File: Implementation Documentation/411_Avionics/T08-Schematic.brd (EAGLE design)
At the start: 65.8 x 25.4 mm, 68 parts, among them IC1 BQ24022, J1 USB-MICROB, J3 JST-PH-2-SMT-RA, U1 LP5907, U2 M25P10-AVMN6TP_TR, U3 LSM9DS0, U5 LTC1998, U6 ATMEGA32U4-AU, X1 8MHz

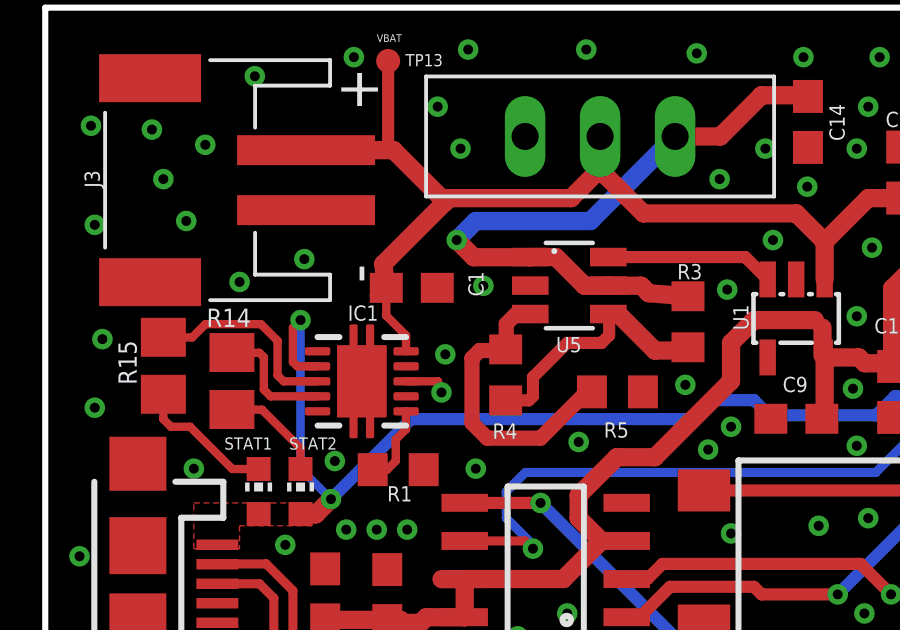
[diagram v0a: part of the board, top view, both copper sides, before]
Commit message: Rerouted /PG pin on BQ24022. Corrected symbol and added to eagle library.
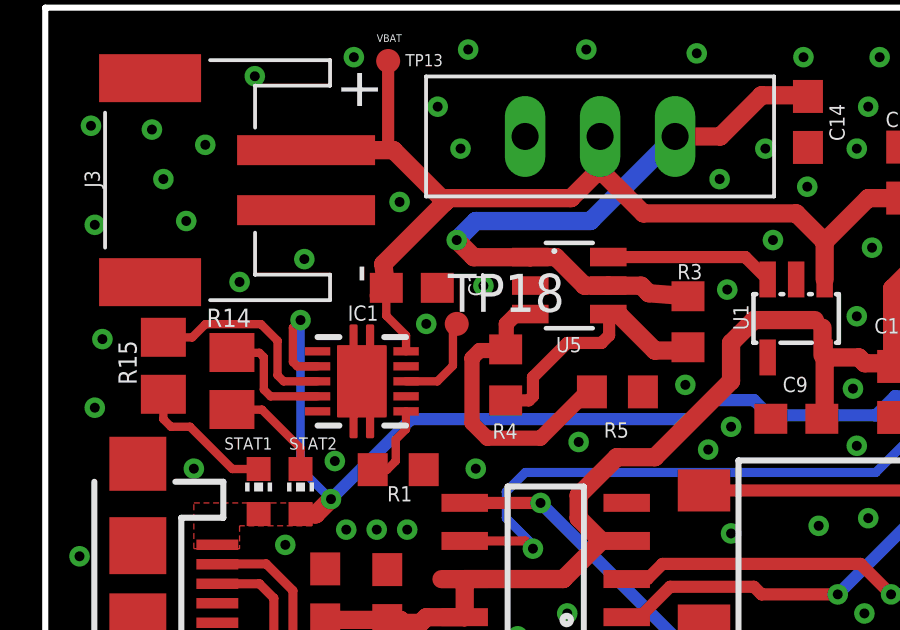
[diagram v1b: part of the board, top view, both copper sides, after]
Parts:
- added TP18: TPTP08R, testpad:TP08R
- IC1: device texas:DRC-S-PVSON-N10 -> tinyav-lib:DRC-S-PVSON-N10
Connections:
- new net N$68: IC1.8, TP18.TP
- net GND: no longer IC1.8
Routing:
- net N$68: track 0.00 -> 3.23 mm
- net GND: track 5.75 -> 4.30 mm
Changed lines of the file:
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@@
 <attribute name="NAME" x="41.906" y="24.562" size="0.508" layer="25" rot="R180"/>
 </element>
-<element name="IC1" library="texas" package="DRC-S-PVSON-N10" value="BQ24022" x="10.552" y="12.944" smashed="yes" rot="R270">
+<element name="IC1" library="tinyav-lib" package="DRC-S-PVSON-N10" value="BQ24022" x="10.552" y="12.944" smashed="yes" rot="R270">
 <attribute name="NAME" x="10.083" y="14.965" size="0.508" layer="25"/>
 </element>
@@
 <attribute name="VALUE" x="53.721" y="21.336" size="0.0254" layer="27"/>
 </element>
+<element name="TP18" library="testpad" package="TP08R" value="TPTP08R" x="13.716" y="14.859">
+<attribute name="TP_SIGNAL_NAME" value="" x="13.716" y="14.859" size="1.778" layer="27" display="off"/>
+</element>
 </elements>
 <signals>
@@
 <contactref element="J1" pad="MT1"/>
 <contactref element="J1" pad="MT2"/>
-<contactref element="IC1" pad="8"/>
 <contactref element="IC1" pad="9"/>
 <contactref element="IC1" pad="7"/>
@@
 <via x="40.894" y="9.906" extent="1-16" drill="0.3302"/>
 <via x="9.652" y="10.287" extent="1-16" drill="0.3302"/>
-<via x="13.335" y="13.843" extent="1-16" drill="0.3302"/>
-<via x="13.208" y="12.573" extent="1-16" drill="0.3302"/>
 <via x="21.336" y="12.827" extent="1-16" drill="0.3302"/>
-<wire x1="12.027" y1="12.944" x2="13.091" y2="12.944" width="0.2794" layer="1"/>
-<wire x1="13.091" y1="12.944" x2="13.208" y2="12.573" width="0.2794" layer="1"/>
 <via x="8.001" y="7.493" extent="1-16" drill="0.3302"/>
 <via x="1.651" y="12.065" extent="1-16" drill="0.3302"/>
@@
 <via x="27.432" y="8.382" extent="1-16" drill="0.3302"/>
 <via x="5.334" y="20.828" extent="1-16" drill="0.3302"/>
+<via x="12.7" y="14.859" extent="1-16" drill="0.3302"/>
+<via x="11.811" y="18.923" extent="1-16" drill="0.3302"/>
 </signal>
 <signal name="N$4">
@@
 <wire x1="53.721" y1="20.955" x2="52.959" y2="21.717" width="0.3048" layer="1"/>
 </signal>
+<signal name="N$68">
+<contactref element="IC1" pad="8"/>
+<contactref element="TP18" pad="TP"/>
+<wire x1="12.027" y1="12.944" x2="13.071" y2="12.944" width="0.2794" layer="1"/>
+<wire x1="13.071" y1="12.944" x2="13.589" y2="13.462" width="0.2794" layer="1"/>
+<wire x1="13.589" y1="13.462" x2="13.589" y2="14.732" width="0.2794" layer="1"/>
+<wire x1="13.589" y1="14.732" x2="13.716" y2="14.859" width="0.2794" layer="1"/>
+</signal>
 </signals>
